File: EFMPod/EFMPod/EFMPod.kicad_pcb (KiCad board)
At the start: 2 copper layers, 47 parts, among them J1 Conn_01x04, J2 UJ2-MBH-1-SMT-TR, J3 Conn_02x18_Odd_Even, SW1 SW_Push, SW2 SW_Push, SW3 SW_Push, U1 AZ1117CH-3_3TRG1, U2 EFM32HG322F64, Y1 24.00MHZ, Y2 Crystal_GND3

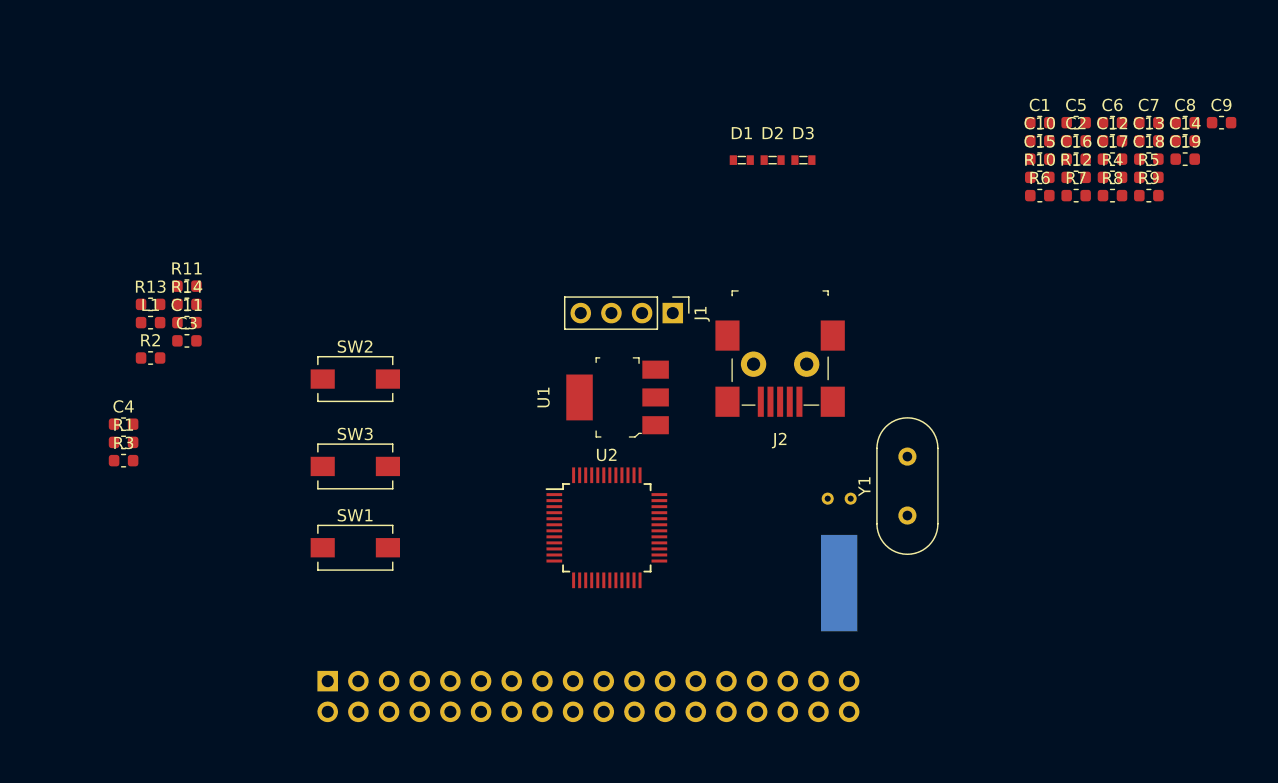
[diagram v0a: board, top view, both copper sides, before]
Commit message: PCB Placement done, routing started
Placement done, signal routing mostly done, board outline generated, mounting holes placed
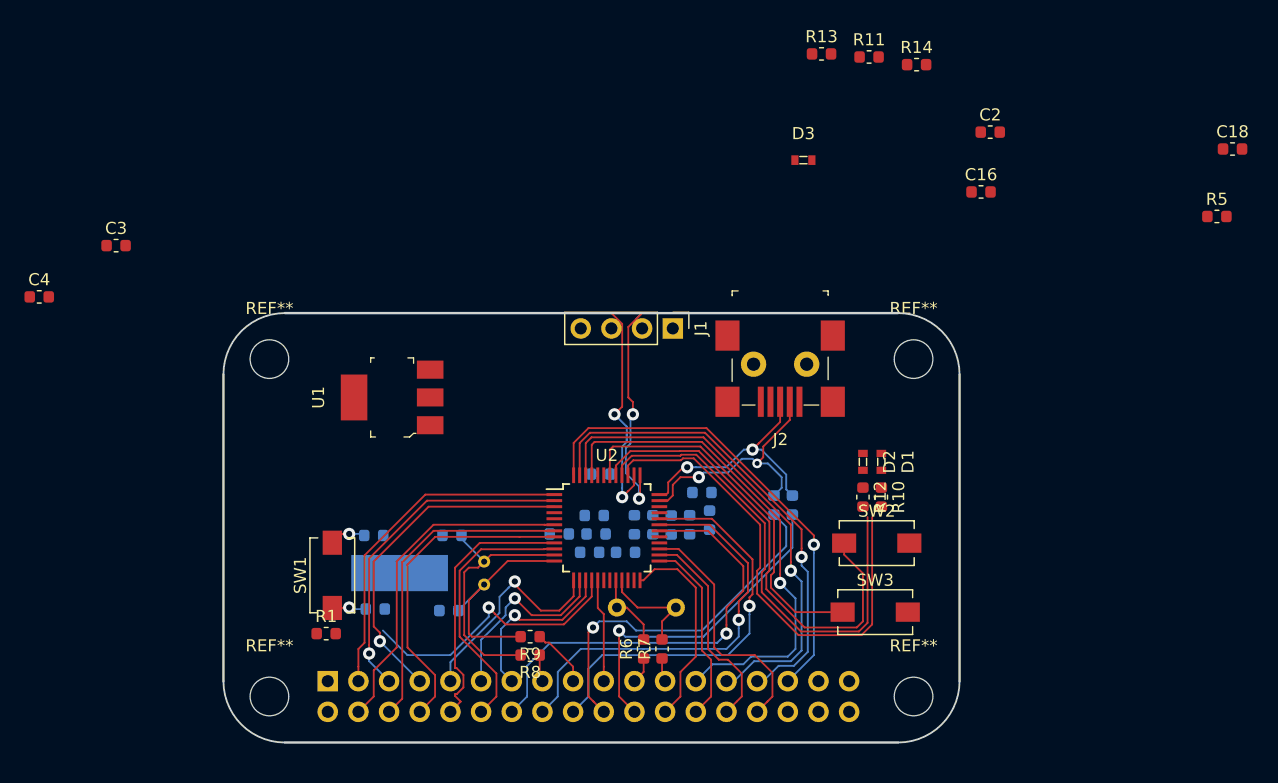
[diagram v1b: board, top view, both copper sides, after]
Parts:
- added REF**: MountingHole_3.2mm_M3, MountingHole:MountingHole_3.2mm_M3, F.Cu at (182.9, 71.1)
- added REF**: MountingHole_3.2mm_M3, MountingHole:MountingHole_3.2mm_M3, F.Cu at (129.5, 71.1)
- added REF**: MountingHole_3.2mm_M3, MountingHole:MountingHole_3.2mm_M3, F.Cu at (129.5, 99.1)
- added REF**: MountingHole_3.2mm_M3, MountingHole:MountingHole_3.2mm_M3, F.Cu at (182.9, 99.1)
- C1, C10, C11, C12, C13, C14, C15, C17, C19, C5, C6, C7, C8, C9, L1, R2, R3, R4: moved to B.Cu
- Y1: value 24.00MHZ -> 24MHz; moved to B.Cu
- moved C19 68.3 mm to (144.7, 85.7), turned to 180 degrees
- moved C1 68.2 mm to (138.3, 91.8)
- moved C17 66.5 mm to (144.4, 91.9), turned to 180 degrees
- moved R14 63.6 mm to (183.1, 46.7)
- moved C9 63.3 mm to (156.1, 87.1), turned to 180 degrees
- moved R9 62.9 mm to (151.1, 94.1), turned to 180 degrees
- moved R8 61.4 mm to (151.1, 95.6), turned to 180 degrees
- moved R11 59.6 mm to (179.2, 46.1)
- moved R13 59.3 mm to (175.3, 45.8)
- moved C6 57.1 mm to (153.5, 85.6)
- moved C13 55.4 mm to (156.4, 84.1), turned to 180 degrees
- moved C8 55.2 mm to (161.3, 84.8), turned to 90 degrees
- moved C7 54.1 mm to (159.8, 84.8), turned to 90 degrees
- moved R3 54.0 mm to (171.3, 83.2), turned to 90 degrees
- moved C12 53.7 mm to (156.6, 85.6), turned to 180 degrees
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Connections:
- Y1 pad 1: /XTALP -> /XTALM
- Y1 pad 2: GNDREF -> /XTALP
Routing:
- net /PE10: track 0.00 -> 41.5 mm, vias 0 -> 1
- net /PE11: track 0.00 -> 40.9 mm, vias 0 -> 1
- net /LED1: track 0.00 -> 40.3 mm
- net /LED0: track 0.00 -> 40.3 mm
- net /PE12: track 0.00 -> 40.3 mm, vias 0 -> 1
- net /PE13: track 0.00 -> 39.7 mm, vias 0 -> 1
- net /SW0: track 0.00 -> 38.8 mm
- net /PC8: track 0.00 -> 36.3 mm, vias 0 -> 1
- net /PC9: track 0.00 -> 35.1 mm, vias 0 -> 1
- net /PC10: track 0.00 -> 34.0 mm, vias 0 -> 1
- net /SW1: track 0.00 -> 30.8 mm
- net /PC14: track 0.00 -> 30.1 mm, vias 0 -> 1
- net /PA0: track 0.00 -> 28.4 mm
- net /PA2: track 0.00 -> 28.3 mm, vias 0 -> 1
- net /PA1: track 0.00 -> 28.2 mm, vias 0 -> 1
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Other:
- board outline added: 61 x 35.6 mm
- net class Default: clearance 0.2 -> 0.1524; trace_width 0.25 -> 0.1524
- net class Power added: clearance 0.254, trace_width 0.254, via_dia 1.016, via_drill 0.508
- net class Signal added: clearance 0.1524, trace_width 0.1524, via_dia 1.016, via_drill 0.508
- rule trace_clearance: 0.2 -> 0.1524
- rule trace_min: 0.2 -> 0.1524
- rule via_min_size: 0.4 -> 0.1524

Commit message: Placement Progress`
Added ARM debug header, some more routing & placement, added correct switches
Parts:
- C15: moved to F.Cu
- C16, C18, R5: moved to B.Cu
- J1: value Conn_01x04 -> Conn_02x05_Odd_Even; footprint Connector_PinHeader_2.54mm:PinHeader_1x04_P2.54mm_Vertical -> Connector_PinHeader_1.27mm:PinHeader_2x05_P1.27mm_Vertical_SMD
- moved C18 67.8 mm to (153.3, 91.9), turned to 180 degrees
- moved R5 51.0 mm to (162.1, 81.4), turned to 90 degrees
- moved C16 48.3 mm to (153.3, 90.4), turned to 180 degrees
- moved C2 47.4 mm to (145.9, 71.6)
- moved C4 36.3 mm to (145.4, 75.8), turned to 270 degrees
- moved R14 35.8 mm to (181.7, 82.5), turned to 270 degrees
- moved R13 33.9 mm to (175.4, 79.8), turned to 270 degrees
- moved R11 33.7 mm to (176.9, 79.8), turned to 270 degrees
- moved C3 33.2 mm to (146.9, 75.8), turned to 270 degrees
- moved D3 26.2 mm to (181.7, 79.6), turned to 270 degrees
- moved J1 5.86 mm to (157.9, 71.5)
- moved C14 1.12 mm to (164.3, 86.0)
- moved C5 1.09 mm to (162.8, 86.0)
- moved C15 1.02 mm to (166.5, 83.6), turned to 0 degrees
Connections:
- J1 pad 2: /DBG_SWCLK -> /DBG_SWDIO
- J1 pad 3: /DBG_SWDIO -> GNDREF
- J1 pad 4: GNDREF -> /DBG_SWCLK
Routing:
- net /~EFM_RESET: track 25.9 -> 58.0 mm
- net /SW1: track 30.8 -> 46.5 mm
- net /XTALM: track 9.08 -> 18.7 mm
- net /DBG_SWCLK: track 19.4 -> 11.6 mm
- net Net-(C11-Pad1): track 0.00 -> 6.82 mm, vias 0 -> 1
- net /SW0: track 38.8 -> 44.7 mm
- net Net-(C15-Pad1): track 0.00 -> 4.42 mm
- net /XTALP: track 6.33 -> 10.7 mm
- net /DBG_SWDIO: track 19.4 -> 15.6 mm
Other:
- rule pad_to_mask_clearance: 0.2 -> 0

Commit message: Layout done
Layout done, silk & gerbers next
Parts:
- C16, C18: moved to F.Cu
- Y1: value 24MHz -> Crystal_GND24; footprint Crystal:Crystal_HC49-U_Vertical -> Crystal:Crystal_SMD_SeikoEpson_FA238-4Pin_3.2x2.5mm_HandSoldering; moved to F.Cu
- moved C16 10.9 mm to (164.2, 89.7)
- moved C18 6.10 mm to (159.4, 92.1), turned to 90 degrees
- moved R7 1.57 mm to (163.6, 95.5), turned to 0 degrees
- moved Y1 1.05 mm to (162.9, 92.7)
- moved R6 0.46 mm to (160.3, 95.5), turned to 0 degrees
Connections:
- Y1 pad 2: /XTALP -> GNDREF
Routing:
- net GNDREF: track 0.00 -> 66.9 mm, vias 0 -> 17
- net +3V3: track 0.00 -> 42.9 mm, vias 0 -> 12
- net VBUS: track 0.00 -> 25.2 mm, vias 0 -> 5
- net Net-(C12-Pad1): track 0.00 -> 9.49 mm, vias 0 -> 2
- net Net-(C14-Pad1): track 0.00 -> 7.96 mm, vias 0 -> 1
- net /PD4: track 17.0 -> 24.8 mm
- net /PD5: track 15.6 -> 21.2 mm
- net /PC10: track 34.0 -> 39.4 mm
- net /~EFM_RESET: track 58.0 -> 62.7 mm
- net /PC9: track 35.1 -> 39.5 mm
- net /PC8: track 36.3 -> 40.6 mm
- net /XTALM: track 18.7 -> 21.7 mm
- net /PC14: track 30.0 -> 27.6 mm
- net /PD6: track 17.6 -> 20.0 mm
- net /XTALP: track 10.7 -> 8.42 mm
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- added copper zone on B.Cu, net +3V3
- added copper zone on F.Cu, net +3V3
- added copper zone on B.Cu, net GNDREF
- added copper zone on B.Cu, net Net-(C12-Pad1)
- added copper zone on B.Cu, net VBUS
- added copper zone on F.Cu, net VBUS
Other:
- net class Power: clearance 0.254 -> 2.032; trace_width 0.254 -> 2.032

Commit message: Rev 1
Done with Rev 1, output generated
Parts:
- added REF**: OSHW-Logo_7.5x8mm_SilkScreen, Symbol:OSHW-Logo_7.5x8mm_SilkScreen, F.Cu at (171.7, 80.4)
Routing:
- net /~EFM_RESET: track 62.7 -> 61.8 mm
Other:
- board text added: "EFM32 Dev Board A. Kowalczyk"
- board text added: "EFM32HG322F64"
- board text added: "For more info: akowalczyk18/Kicad/EFMPod"
- board text added: "REV"
- board text added: "SN"
- board text added: "VBUS GND"
- board text added: "akowalczyk18@gmail.com"
